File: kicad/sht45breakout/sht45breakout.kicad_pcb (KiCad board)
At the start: 2 copper layers, 15 x 15 mm, 5 parts, among them J1 Conn_01x04, U1 SHT45

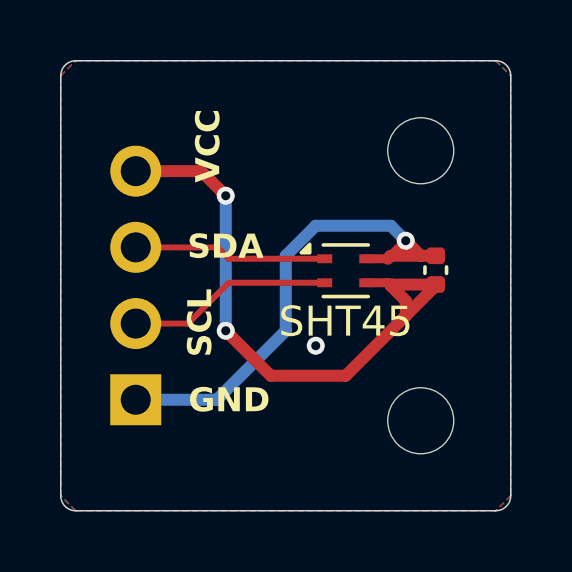
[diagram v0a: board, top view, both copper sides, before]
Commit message: add 4.7k pullup resistors and solder jumpers to enable them (by default they are disabled)
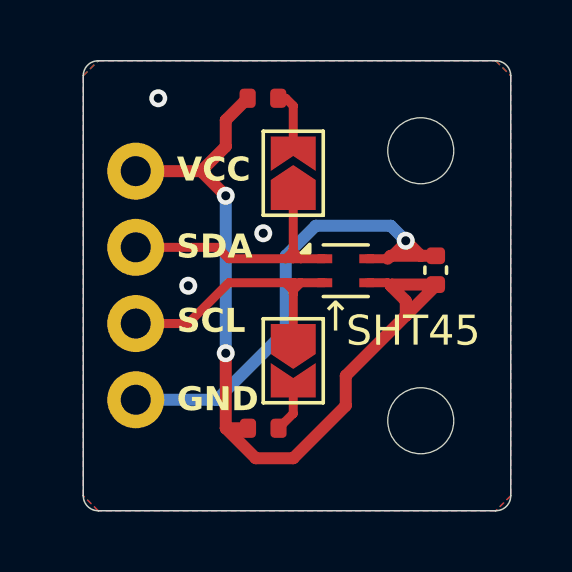
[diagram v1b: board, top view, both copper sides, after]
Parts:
- added JP1: enable_pullup1, Jumper:SolderJumper-2_P1.3mm_Open_TrianglePad1.0x1.5mm, F.Cu at (118.8, 77.8)
- added JP2: enable_pullup2, Jumper:SolderJumper-2_P1.3mm_Open_TrianglePad1.0x1.5mm, F.Cu at (118.8, 84.0)
- added R1: 4.7k, foxisfrickellibrary:R_0402_modsilkscreen, F.Cu at (117.7, 75.2)
- added R2: 4.7k, foxisfrickellibrary:R_0402_modsilkscreen, F.Cu at (117.8, 86.2)
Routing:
- net VCC: track 20.3 -> 28.9 mm
- net /SDA: track 6.46 -> 9.39 mm
- net /SCL: track 6.86 -> 9.55 mm
- net Net-(JP1-B): track 0.00 -> 2.13 mm
- net Net-(JP2-B): track 0.00 -> 1.73 mm
- net GND: vias 2 -> 4
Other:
- board size 15 x 15 mm -> 14.2 x 15 mm
- board text added: "SHT45 breakout"
- board text added: "↑"
